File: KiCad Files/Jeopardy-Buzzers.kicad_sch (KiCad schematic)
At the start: 29 parts, among them J1 USB_C_Receptacle_USB2.0_14P, J2 Conn_01x02_Pin, J3 Conn_01x03_Socket, J4 Conn_01x03_Socket, J5 Conn_02x04_Odd_Even, U1 CH32V003FxUx, U2 CH340N, U3 NRF24L01_Breakout, U5 AMS1117-3.3, Y1 Crystal_24MHz

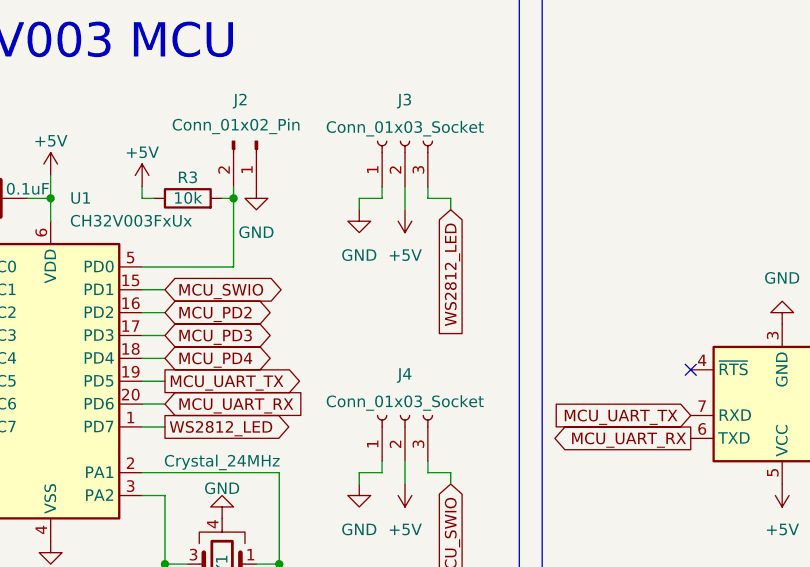
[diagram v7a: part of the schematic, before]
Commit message: Had the pinout for the addressable RGB cable backwards
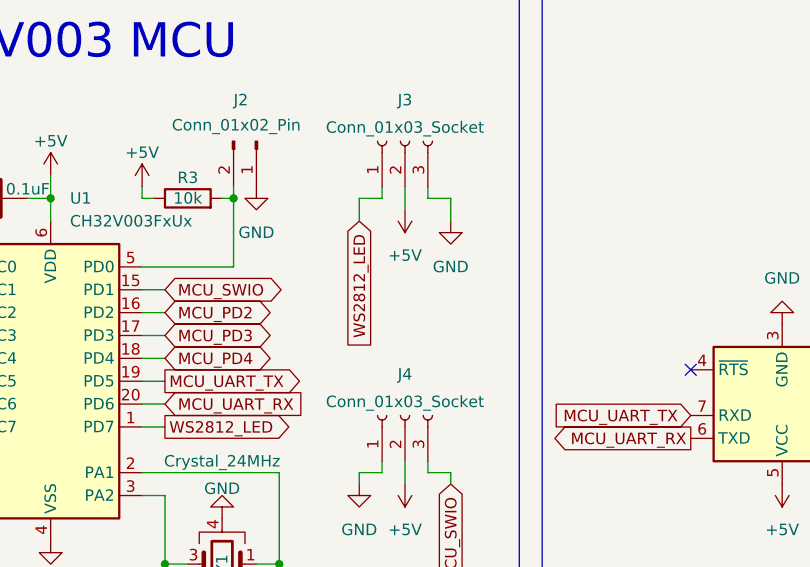
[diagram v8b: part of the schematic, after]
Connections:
- net GND: now also J3.3 (Pin_3); no longer J3.1 (Pin_1)
- net WS2812_LED: now also J3.1 (Pin_1); no longer J3.3 (Pin_3)
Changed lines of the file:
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@@
 	(wire
 		(pts
+			(xy 156.21 36.83) (xy 156.21 39.37)
+		)
+		(stroke
+			(width 0)
+			(type default)
+		)
+	)
+	(wire
+		(pts
 			(xy 134.62 88.9) (xy 140.97 88.9)
 		)
@@
 	(wire
 		(pts
-			(xy 166.37 36.83) (xy 166.37 38.1)
-		)
-		(stroke
-			(width 0)
-			(type default)
-		)
-	)
-	(wire
-		(pts
 			(xy 49.53 85.09) (xy 52.07 85.09)
 		)
@@
 	(wire
 		(pts
-			(xy 156.21 36.83) (xy 156.21 38.1)
-		)
-		(stroke
-			(width 0)
-			(type default)
-		)
-	)
-	(wire
-		(pts
 			(xy 92.71 87.63) (xy 93.98 87.63)
 		)
@@
 	(wire
 		(pts
+			(xy 166.37 36.83) (xy 166.37 39.37)
+		)
+		(stroke
+			(width 0)
+			(type default)
+		)
+	)
+	(wire
+		(pts
 			(xy 134.62 69.85) (xy 134.62 77.47)
 		)
@@
 		)
 	)
-	(global_label "WS2812_LED"
-		(shape input)
-		(at 166.37 38.1 270)
+	(global_label "MCU_PC0"
+		(shape bidirectional)
+		(at 90.17 38.1 90)
 		(fields_autoplaced yes)
 		(effects
@@
 				(size 1.27 1.27)
 			)
-			(justify right)
+			(justify left)
 		)
 		(property "Intersheetrefs" "${INTERSHEET_REFS}"
-			(at 166.37 52.9988 90)
+			(at 90.17 25.2345 90)
 			(effects
 				(font
 					(size 1.27 1.27)
 				)
-				(justify right)
+				(justify left)
 				(hide yes)
 			)
@@
 	(global_label "MCU_PC0"
 		(shape bidirectional)
-		(at 90.17 38.1 90)
+		(at 109.22 44.45 180)
 		(fields_autoplaced yes)
 		(effects
@@
 				(size 1.27 1.27)
 			)
-			(justify left)
+			(justify right)
 		)
 		(property "Intersheetrefs" "${INTERSHEET_REFS}"
-			(at 90.17 25.2345 90)
+			(at 96.3545 44.45 0)
 			(effects
 				(font
 					(size 1.27 1.27)
 				)
-				(justify left)
+				(justify right)
 				(hide yes)
 			)
 		)
 	)
-	(global_label "MCU_PC0"
-		(shape bidirectional)
-		(at 109.22 44.45 180)
+	(global_label "WS2812_LED"
+		(shape input)
+		(at 156.21 39.37 270)
 		(fields_autoplaced yes)
 		(effects
@@
 		)
 		(property "Intersheetrefs" "${INTERSHEET_REFS}"
-			(at 96.3545 44.45 0)
+			(at 156.21 54.2688 90)
 			(effects
 				(font
@@
 	(symbol
 		(lib_id "power:GND")
-		(at 156.21 38.1 0)
+		(at 166.37 39.37 0)
 		(unit 1)
 		(exclude_from_sim no)
@@
 		(fields_autoplaced yes)
 		(property "Reference" "#PWR020"
-			(at 156.21 44.45 0)
+			(at 166.37 45.72 0)
 			(effects
 				(font
@@
 		)
 		(property "Value" "GND"
-			(at 156.21 43.18 0)
+			(at 166.37 44.45 0)
 			(effects
 				(font
@@
 		)
 		(property "Footprint" ""
-			(at 156.21 38.1 0)
+			(at 166.37 39.37 0)
 			(effects
 				(font
@@
 		)
 		(property "Datasheet" ""
-			(at 156.21 38.1 0)
+			(at 166.37 39.37 0)
 			(effects
 				(font
@@
 		)
 		(property "Description" "Power symbol creates a global label with name \"GND\" , ground"
-			(at 156.21 38.1 0)
+			(at 166.37 39.37 0)
 			(effects
 				(font
